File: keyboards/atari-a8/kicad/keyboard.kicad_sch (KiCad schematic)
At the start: 140 parts, among them SW201 ESC, SW202 1, SW203 2, SW204 3, SW205 4, SW206 5, SW207 6, SW208 7, SW209 8, SW210 9, SW211 0, SW212 LT, SW213 GT, SW214 BS, SW215 C_UP, SW216 C_LEFT, SW217 C_DOWN, SW218 C_RIGHT, SW219 TAB, SW220 Q, SW221 W, SW222 E, SW223 R, SW224 T, SW225 Y, SW226 U, SW227 I, SW228 O, SW229 P, SW230 DASH, SW231 EQUAL, SW232 RET, SW233 HELP, SW234 RESET, SW235 OPTION, SW236 SELECT, SW237 CTRL, SW238 A, SW239 S, SW240 D, SW241 F, SW242 G, SW243 H, SW244 J, SW245 K, SW246 L, SW247 SEMI, SW248 PLUS, SW249 ASTRIX, SW250 CAPS, SW251 START, SW252 POWER, SW253 MENU, SW254 TURBO, SW255 FN, SW256 LSHIFT, SW257 Z, SW258 X, SW259 C, SW260 V, SW261 B, SW262 N, SW263 M, SW264 COMMA, SW265 PERIOD, SW266 SLASH, SW267 RSHIFT, SW268 INV, SW269 BREAK, SW270 SPACE

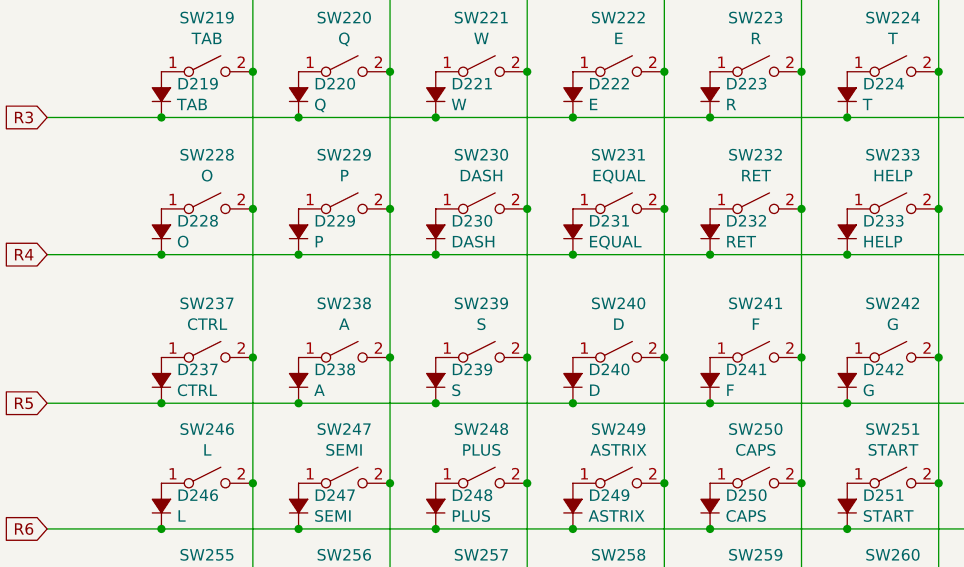
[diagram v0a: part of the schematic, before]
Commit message: Shifted the code to use the keyboard_layout file more
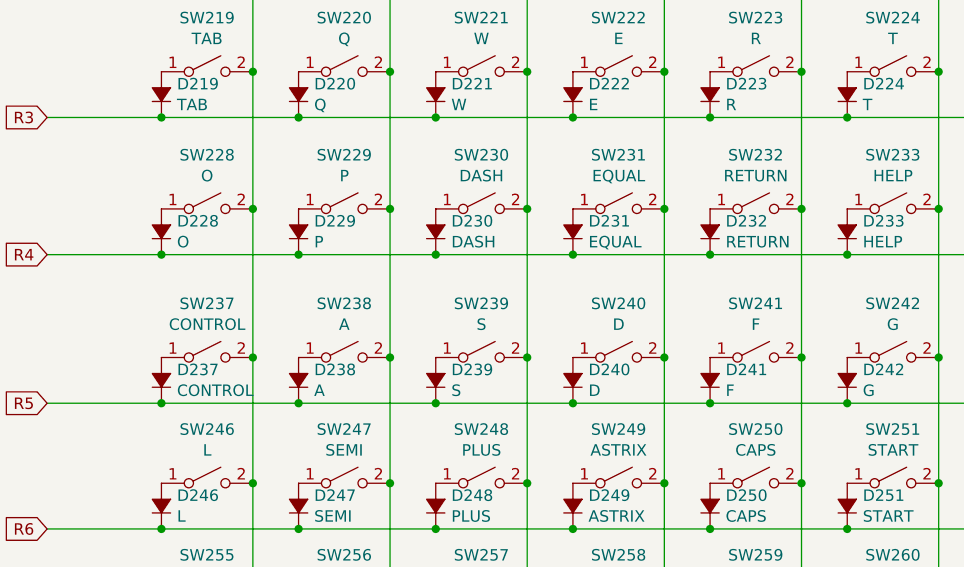
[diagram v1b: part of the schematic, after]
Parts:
- D232, SW232: value RET -> RETURN
- D237, SW237: value CTRL -> CONTROL
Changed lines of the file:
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@@
       (effects (font (size 1.27 1.27)) (justify right))
     )
-    (property "Value" "RET" (id 1) (at 201.1172 86.233 90)
+    (property "Value" "RETURN" (id 1) (at 201.1172 86.233 90)
       (effects (font (size 1.27 1.27)) (justify right))
     )
@@
       (effects (font (size 1.27 1.27)) (justify right))
     )
-    (property "Value" "CTRL" (id 1) (at 140.1572 102.743 90)
+    (property "Value" "CONTROL" (id 1) (at 140.1572 102.743 90)
       (effects (font (size 1.27 1.27)) (justify right))
     )
@@
     (in_bom yes) (on_board yes)
     (property "Reference" "SW232" (id 0) (at 204.47 76.581 0))
-    (property "Value" "RET" (id 1) (at 204.47 78.8924 0))
+    (property "Value" "RETURN" (id 1) (at 204.47 78.8924 0))
     (property "Footprint" "Button_Switch_Keyboard:SW_Cherry_MX_1.50u_PCB" (id 2) (at 204.47 82.55 0)
       (effects (font (size 1.27 1.27)) hide)
@@
     (in_bom yes) (on_board yes)
     (property "Reference" "SW237" (id 0) (at 143.51 93.091 0))
-    (property "Value" "CTRL" (id 1) (at 143.51 95.4024 0))
+    (property "Value" "CONTROL" (id 1) (at 143.51 95.4024 0))
     (property "Footprint" "Button_Switch_Keyboard:SW_Cherry_MX_2.00u_PCB" (id 2) (at 143.51 99.06 0)
       (effects (font (size 1.27 1.27)) hide)
